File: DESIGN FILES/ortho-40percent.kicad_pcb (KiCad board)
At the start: 2 copper layers, 229 x 81 mm, 134 parts, among them J1 USB-C_Receptacle-24, SW1 SW_NO_4-Pin, SW10 CherryMX, SW11 CherryMX, SW12 CherryMX, SW13 CherryMX, SW14 CherryMX, SW15 CherryMX, SW16 CherryMX, SW17 CherryMX, SW18 CherryMX, SW19 CherryMX, SW2 CherryMX, SW20 CherryMX, SW21 CherryMX, SW22 CherryMX, SW23 CherryMX, SW24 CherryMX, SW25 CherryMX, SW26 CherryMX, SW27 CherryMX, SW28 CherryMX, SW29 CherryMX, SW3 CherryMX, SW30 CherryMX, SW31 CherryMX, SW32 CherryMX, SW33 CherryMX, SW34 CherryMX, SW35 CherryMX, SW36 CherryMX, SW37 CherryMX, SW38 CherryMX, SW39 CherryMX, SW4 CherryMX, SW40 CherryMX, SW41 CherryMX, SW42 CherryMX, SW43 CherryMX, SW44 CherryMX, SW45 CherryMX, SW46 CherryMX, SW47 CherryMX, SW48 CherryMX, SW49 CherryMX, SW5 CherryMX, SW50 CherryMX, SW51 CherryMX, SW6 CherryMX, SW7 CherryMX, SW8 CherryMX, SW9 CherryMX, U1 U_TPD4E05U06DQAR, U2 U_ATmega32u4-MU, Y1 XTAL_4Lead

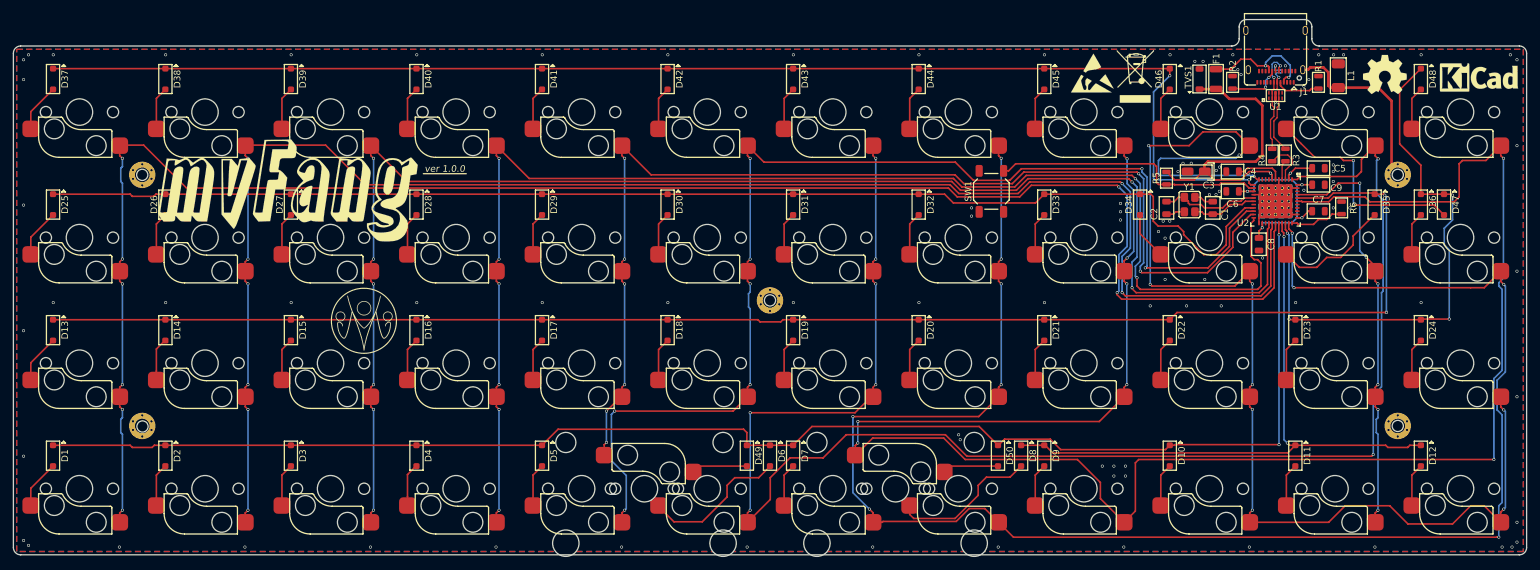
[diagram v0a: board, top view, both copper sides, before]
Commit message: Consolidating design files
Added directory to store design separate from production files
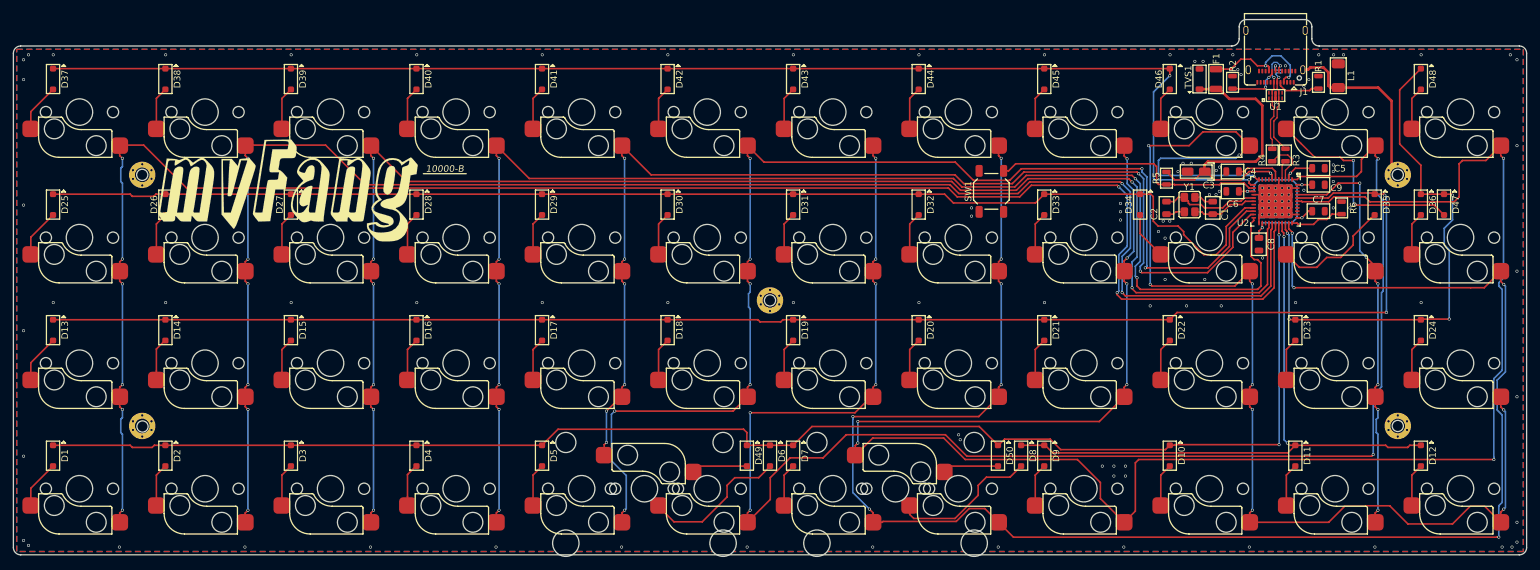
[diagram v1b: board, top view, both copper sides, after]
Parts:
- removed the G*** at (93.0, 204.5)
- removed REF**: KiCAD Logo, Symbols:Symbol_KiCAD-Logo_CopperAndSilkScreenTop
- removed REF***: ESD-Logo_6.6x6mm_SilkScreen, Symbols:ESD-Logo_6.6x6mm_SilkScreen
- removed REF***: OSHW-Symbol_6.7x6mm_SilkScreen, Symbols:OSHW-Symbol_6.7x6mm_SilkScreen
- removed REF***: WEEE-Logo_5.6x8mm_SilkScreen, Symbols:WEEE-Logo_5.6x8mm_SilkScreen
- C1, C2: footprint ortho-40percent:C_0805 -> master-vampire:C_0805
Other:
- board text added: "10000-B"
- board text removed: "ver 1.0.0"

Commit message: Added stencil guide holes
Added 2.6mm dia guide holes at 10mm spacings to board to help with stencil alignment
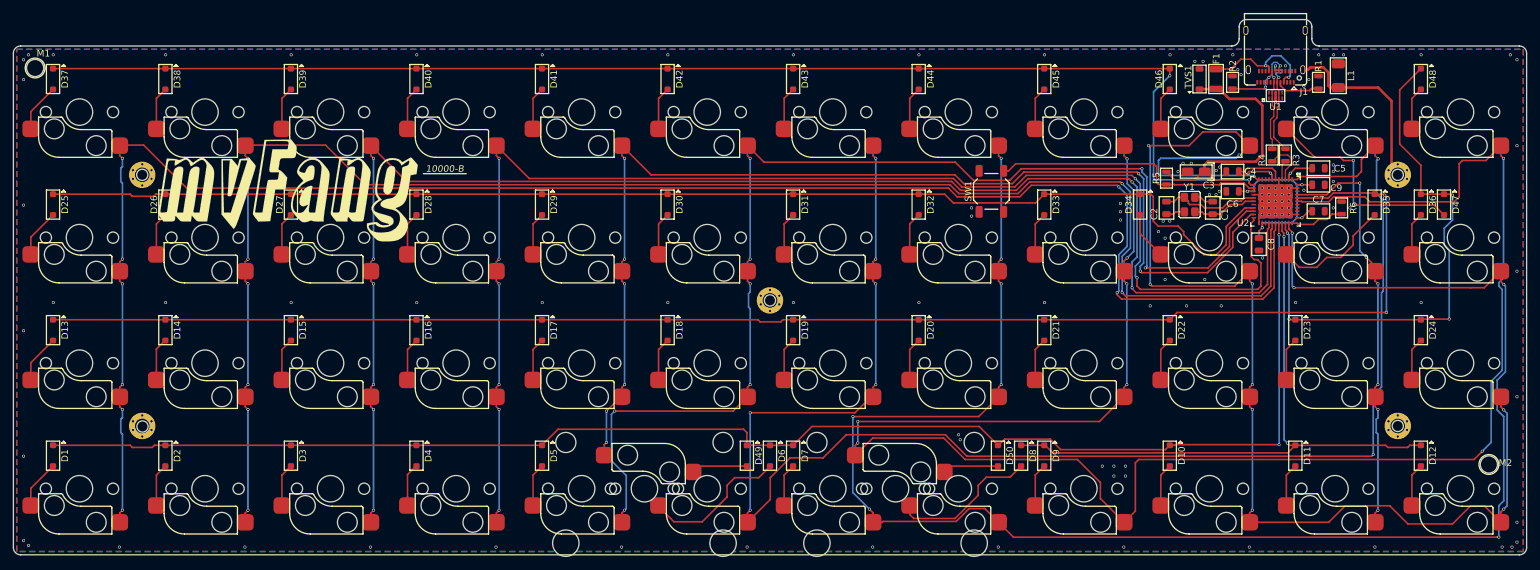
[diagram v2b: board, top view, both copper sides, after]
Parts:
- added M1: M_StencilGuide, master-vampire:STENCIL_GUIDE_HOLE, F.Cu at (43.2, 166.2)
- added M2: M_StencilGuide, master-vampire:STENCIL_GUIDE_HOLE, F.Cu at (263.2, 226.2)
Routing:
- net /COL8: track 286.0 -> 284.2 mm
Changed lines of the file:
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@@
     (thickness 1.6)
     (drawings 79)
-    (tracks 1187)
+    (tracks 1190)
     (zones 0)
-    (modules 129)
+    (modules 131)
     (nets 96)
   )
@@
     )
   )
+  (module master-vampire:STENCIL_GUIDE_HOLE (layer F.Cu)
+    (at 43.25 166.25)
+    (attr virtual)
+    (fp_text reference M1 (at 1.25 -2.2) (layer F.SilkS)
+      (effects (font (size 1 1) (thickness 0.15)))
+    )
+    (fp_text value M_StencilGuide (at 0 2.1) (layer F.Fab)
+      (effects (font (size 1 1) (thickness 0.15)))
+    )
+    (fp_text user %R (at 1.25 -2.2) (layer F.Fab)
+      (effects (font (size 1 1) (thickness 0.15)))
+    )
+    (fp_circle (center 0 0) (end 1.5 0) (layer F.SilkS) (width 0.12))
+    (pad "" np_thru_hole circle (at 0 0) (size 2.6 2.6) (drill 2.6) (layers *.Cu *.Paste *.Mask))
+  )
+  (module master-vampire:STENCIL_GUIDE_HOLE (layer F.Cu)
+    (at 263.25 226.25)
+    (attr virtual)
+    (fp_text reference M2 (at 2.5 -0.25) (layer F.SilkS)
+      (effects (font (size 1 1) (thickness 0.15)))
+    )
+    (fp_text value M_StencilGuide (at 0 2.1) (layer F.Fab)
+      (effects (font (size 1 1) (thickness 0.15)))
+    )
+    (fp_circle (center 0 0) (end 1.5 0) (layer F.SilkS) (width 0.12))
+    (fp_text user %R (at 2.5 -0.25) (layer F.Fab)
+      (effects (font (size 1 1) (thickness 0.15)))
+    )
+    (pad "" np_thru_hole circle (at 0 0) (size 2.6 2.6) (drill 2.6) (layers *.Cu *.Paste *.Mask))
+  )
   (dimension 12.54 (width 0.15) (layer F.Fab)
     (gr_text "12.540 mm" (at 46.23 245.05) (layer F.Fab)
@@
   (segment (start 265.05 197) (end 265.05 198.55) (width 0.25) (layer F.Cu) (net 83))
   (segment (start 265.05 198.55) (end 265.5 199) (width 0.25) (layer F.Cu) (net 83))
-  (segment (start 265.75 199.25) (end 265.5 199) (width 0.25) (layer B.Cu) (net 83))
-  (segment (start 265.75 212.25) (end 265.75 199.25) (width 0.25) (layer B.Cu) (net 83))
-  (segment (start 264.75 232.5) (end 265.25 232) (width 0.25) (layer B.Cu) (net 83))
-  (segment (start 264.75 237.25) (end 264.75 232.5) (width 0.25) (layer B.Cu) (net 83))
-  (segment (start 265.25 232) (end 265.25 218.75) (width 0.25) (layer B.Cu) (net 83))
-  (segment (start 265.25 218.75) (end 264.5 218) (width 0.25) (layer B.Cu) (net 83))
-  (segment (start 264.5 218) (end 264.5 213.5) (width 0.25) (layer B.Cu) (net 83))
-  (segment (start 264.5 213.5) (end 265.75 212.25) (width 0.25) (layer B.Cu) (net 83))
   (via (at 169.5 233) (size 0.45) (drill 0.3) (layers F.Cu B.Cu) (net 83))
   (segment (start 170.05 233.55) (end 169.5 233) (width 0.25) (layer F.Cu) (net 83))
@@
   (segment (start 167 230.5) (end 167 219.318198) (width 0.25) (layer B.Cu) (net 83))
   (via (at 167 219) (size 0.45) (drill 0.3) (layers F.Cu B.Cu) (net 83))
+  (segment (start 265.75 199.25) (end 265.5 199) (width 0.25) (layer B.Cu) (net 83))
+  (segment (start 265.75 212.25) (end 265.75 199.25) (width 0.25) (layer B.Cu) (net 83))
+  (segment (start 264.75 237.25) (end 264.75 232.5) (width 0.25) (layer B.Cu) (net 83))
+  (segment (start 265.5 219) (end 264.5 218) (width 0.25) (layer B.Cu) (net 83))
+  (segment (start 264.75 232.5) (end 265.5 231.75) (width 0.25) (layer B.Cu) (net 83))
+  (segment (start 264.5 218) (end 264.5 213.5) (width 0.25) (layer B.Cu) (net 83))
+  (segment (start 265.5 231.75) (end 265.5 219) (width 0.25) (layer B.Cu) (net 83))
+  (segment (start 264.5 213.5) (end 265.75 212.25) (width 0.25) (layer B.Cu) (net 83))
   (via (at 227.71 182.67) (size 0.45) (drill 0.3) (layers F.Cu B.Cu) (net 84))
   (segment (start 228.46 183.12) (end 228.16 183.12) (width 0.25) (layer F.Cu) (net 84))
@@
   (segment (start 265.05 235) (end 265.05 233.45) (width 0.25) (layer F.Cu) (net 84))
   (segment (start 265.05 233.45) (end 265.5 233) (width 0.25) (layer F.Cu) (net 84))
-  (segment (start 265.75 232.75) (end 265.5 233) (width 0.25) (layer B.Cu) (net 84))
-  (segment (start 265.5 218) (end 265.75 218.25) (width 0.25) (layer B.Cu) (net 84))
-  (segment (start 265.75 218.25) (end 265.75 232.75) (width 0.25) (layer B.Cu) (net 84))
   (segment (start 224.8 199.25) (end 227.05 197) (width 0.25) (layer F.Cu) (net 84))
   (via (at 212 199) (size 0.45) (drill 0.3) (layers F.Cu B.Cu) (net 84))
@@
   (segment (start 213.25 182.25) (end 213.5 182.5) (width 0.25) (layer B.Cu) (net 84))
   (segment (start 213.5 182.5) (end 227.54 182.5) (width 0.25) (layer B.Cu) (net 84))
+  (segment (start 266 232.5) (end 265.5 233) (width 0.25) (layer B.Cu) (net 84))
+  (segment (start 265.5 218) (end 266 218.5) (width 0.25) (layer B.Cu) (net 84))
+  (segment (start 266 218.5) (end 266 232.5) (width 0.25) (layer B.Cu) (net 84))
   (segment (start 208.13 196.92) (end 208.05 197) (width 0.25) (layer F.Cu) (net 85))
   (via (at 208.46 214.17) (size 0.45) (drill 0.3) (layers F.Cu B.Cu) (net 85))
@@
   (segment (start 239.76641 185.75) (end 244.5 185.75) (width 0.25) (layer F.Cu) (net 85))
   (segment (start 244.5 185.75) (end 245.25 186.5) (width 0.25) (layer F.Cu) (net 85))
-  (via (at 264 225.5) (size 0.45) (drill 0.3) (layers F.Cu B.Cu) (net 85))
-  (segment (start 265.46 179.92) (end 265.46 198.04) (width 0.25) (layer B.Cu) (net 85))
-  (segment (start 265.46 198.04) (end 264.75 198.75) (width 0.25) (layer B.Cu) (net 85))
-  (segment (start 264.75 199.25) (end 265.25 199.75) (width 0.25) (layer B.Cu) (net 85))
-  (segment (start 264.75 198.75) (end 264.75 199.25) (width 0.25) (layer B.Cu) (net 85))
-  (segment (start 265.25 212) (end 264 213.25) (width 0.25) (layer B.Cu) (net 85))
-  (segment (start 265.25 199.75) (end 265.25 212) (width 0.25) (layer B.Cu) (net 85))
-  (segment (start 264 213.25) (end 264 225.181802) (width 0.25) (layer B.Cu) (net 85))
-  (segment (start 264 225.181802) (end 264 225.5) (width 0.25) (layer B.Cu) (net 85))
-  (segment (start 209.75 226) (end 210.25 225.5) (width 0.25) (layer F.Cu) (net 85))
-  (segment (start 209.75 233.3) (end 209.75 226) (width 0.25) (layer F.Cu) (net 85))
-  (segment (start 208.05 235) (end 209.75 233.3) (width 0.25) (layer F.Cu) (net 85))
-  (segment (start 264 225.5) (end 210.25 225.5) (width 0.25) (layer F.Cu) (net 85))
   (segment (start 206.900463 233.850463) (end 208.05 235) (width 0.25) (layer F.Cu) (net 85))
   (segment (start 204.46 231.41) (end 206.900463 233.850463) (width 0.25) (layer F.Cu) (net 85))
@@
   (segment (start 208.05 216) (end 204.3 219.75) (width 0.25) (layer F.Cu) (net 85))
   (segment (start 204.3 219.75) (end 167.750056 219.75) (width 0.25) (layer F.Cu) (net 85))
+  (via (at 262.250004 224.25) (size 0.45) (drill 0.3) (layers F.Cu B.Cu) (net 85))
+  (segment (start 263.588304 222.9117) (end 262.475003 224.025001) (width 0.25) (layer B.Cu) (net 85))
+  (segment (start 263.588304 213.661696) (end 263.588304 222.9117) (width 0.25) (layer B.Cu) (net 85))
+  (segment (start 264.75 199.25) (end 265.25 199.75) (width 0.25) (layer B.Cu) (net 85))
+  (segment (start 265.25 199.75) (end 265.25 212) (width 0.25) (layer B.Cu) (net 85))
+  (segment (start 265.46 179.92) (end 265.46 198.04) (width 0.25) (layer B.Cu) (net 85))
+  (segment (start 265.46 198.04) (end 264.75 198.75) (width 0.25) (layer B.Cu) (net 85))
+  (segment (start 264.75 198.75) (end 264.75 199.25) (width 0.25) (layer B.Cu) (net 85))
+  (segment (start 265.25 212) (end 263.588304 213.661696) (width 0.25) (layer B.Cu) (net 85))
+  (segment (start 262.475003 224.025001) (end 262.250004 224.25) (width 0.25) (layer B.Cu) (net 85))
+  (segment (start 261.000004 225.5) (end 262.025005 224.474999) (width 0.25) (layer F.Cu) (net 85))
+  (segment (start 262.025005 224.474999) (end 262.250004 224.25) (width 0.25) (layer F.Cu) (net 85))
+  (segment (start 210.25 225.5) (end 261.000004 225.5) (width 0.25) (layer F.Cu) (net 85))
+  (segment (start 209.75 226) (end 210.25 225.5) (width 0.25) (layer F.Cu) (net 85))
+  (segment (start 209.75 233.3) (end 209.75 226) (width 0.25) (layer F.Cu) (net 85))
+  (segment (start 208.05 235) (end 209.75 233.3) (width 0.25) (layer F.Cu) (net 85))
   (segment (start 234.26 185.42) (end 238.71 185.42) (width 0.25) (layer F.Cu) (net 86))
   (segment (start 238.71 185.42) (end 239.46 184.67) (width 0.25) (layer F.Cu) (net 86))
